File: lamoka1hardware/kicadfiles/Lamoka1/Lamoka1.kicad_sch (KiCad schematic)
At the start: 0 parts

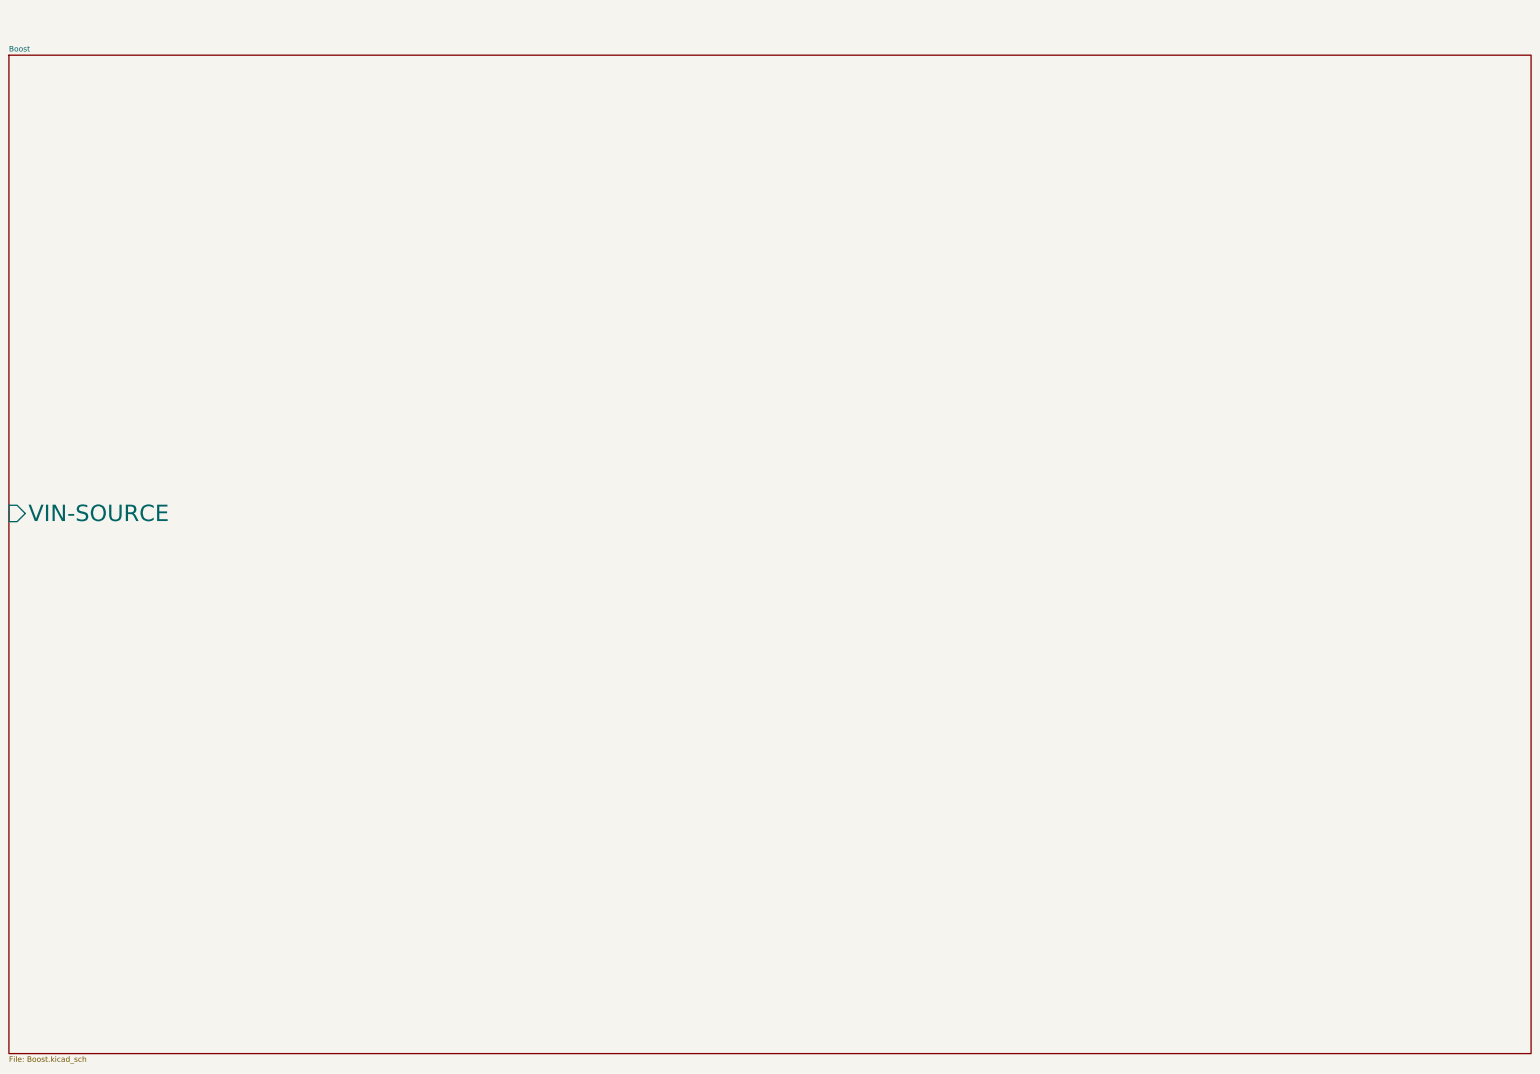
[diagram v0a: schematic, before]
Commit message: ADD the schematic for testing the boost section is all done and configured
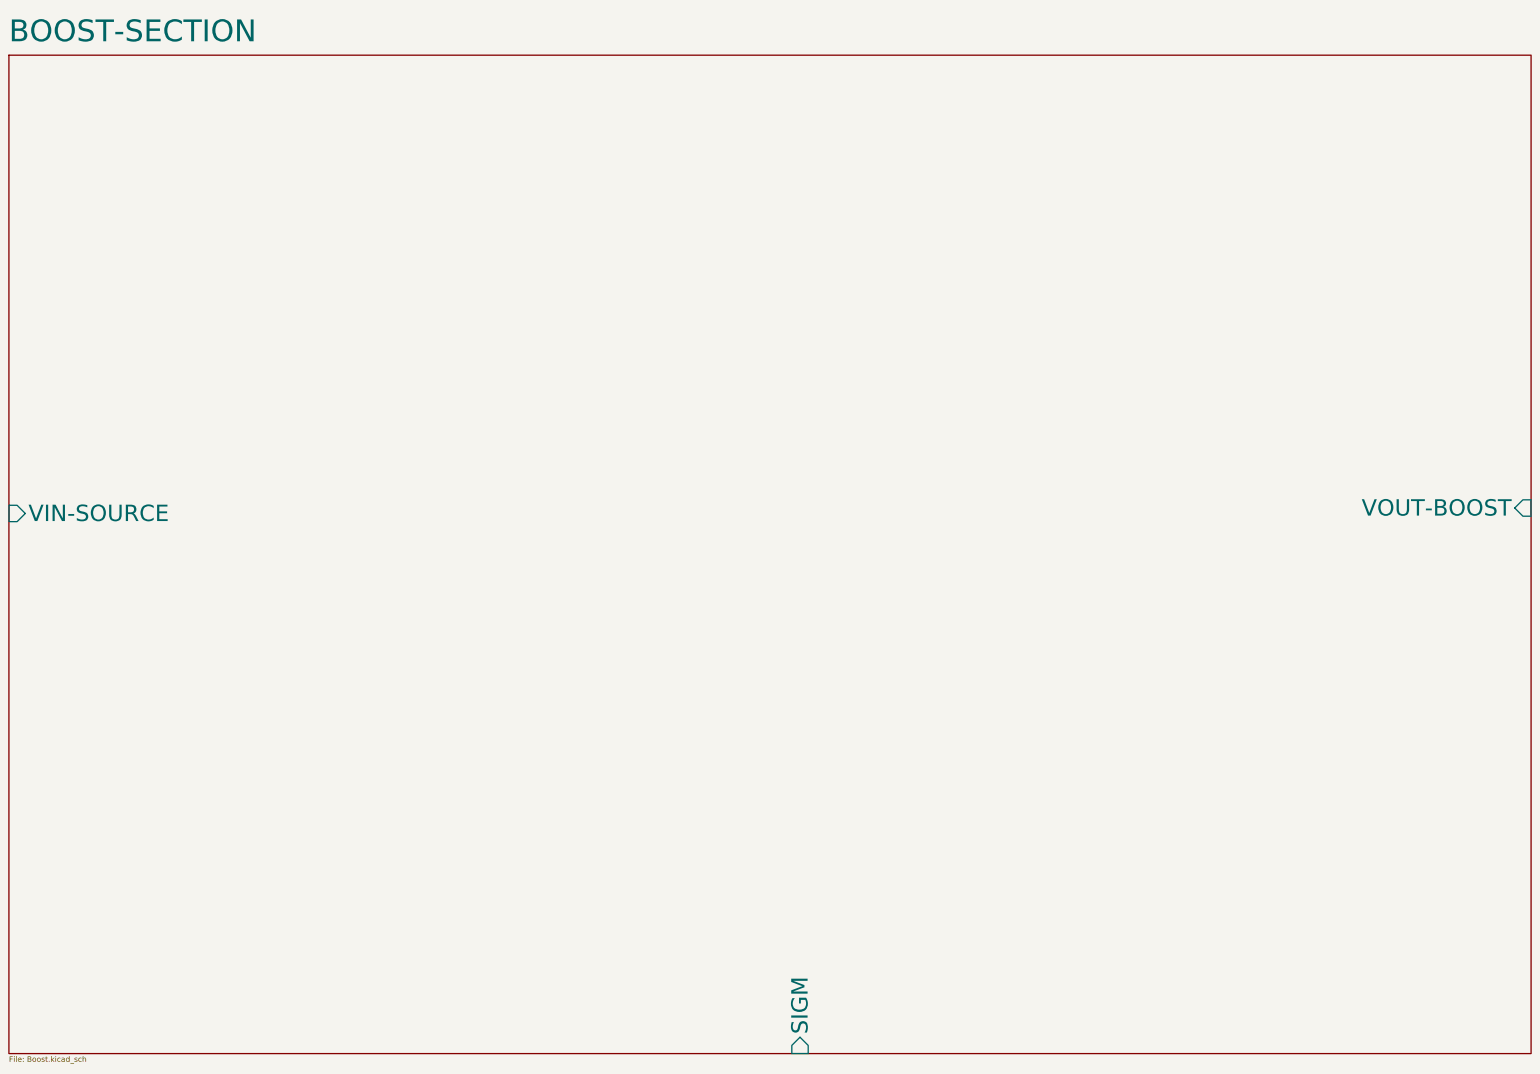
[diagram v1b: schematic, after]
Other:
- sheet Boost renamed BOOST-SECTION
- sheet BOOST-SECTION ports: added SIGM, VOUT-BOOST; removed none
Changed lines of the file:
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@@
 			(color 0 0 0 0)
 		)
-		(property "Sheetname" "Boost"
-			(at 26.67 23.4184 0)
+		(property "Sheetname" "BOOST-SECTION"
+			(at 26.67 21.5134 0)
 			(show_name no)
 			(do_not_autoplace no)
 			(effects
 				(font
-					(size 1.27 1.27)
+					(size 5.08 5.08)
 				)
 				(justify left bottom)
@@
 			)
 		)
+		(pin "SIGM" input
+			(at 210.82 256.54 270)
+			(effects
+				(font
+					(size 3.81 3.81)
+				)
+				(justify left)
+			)
+		)
+		(pin "VOUT-BOOST" input
+			(at 381 129.54 0)
+			(effects
+				(font
+					(size 3.81 3.81)
+				)
+				(justify right)
+			)
+		)
